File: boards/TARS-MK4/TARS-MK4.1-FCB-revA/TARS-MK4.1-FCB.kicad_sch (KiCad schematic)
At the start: 57 parts, among them J101 U.FL, J102 Molex_SlimStack_2091680401_2x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, J103 Molex_SlimStack_2091680401_2x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, J104 Molex_SlimStack_Plug_55091047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, J105 Molex_SlimStack_Plug_55091047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, J106 Conn_01x03, J107 Conn_01x02, J108 Conn_01x06, J109 Conn_01x03, Q101 SSM3K16FU, SW101 FSMSM Switch, U101 MS5611-01BA03, U102 LSM6DSLTR, U103 MAX-M10S, U104 BNO086, U105 LIS3MDL, U106 KX134-1211, U107 Teensy4.1, U108 BME688, Y101 32.768kHz

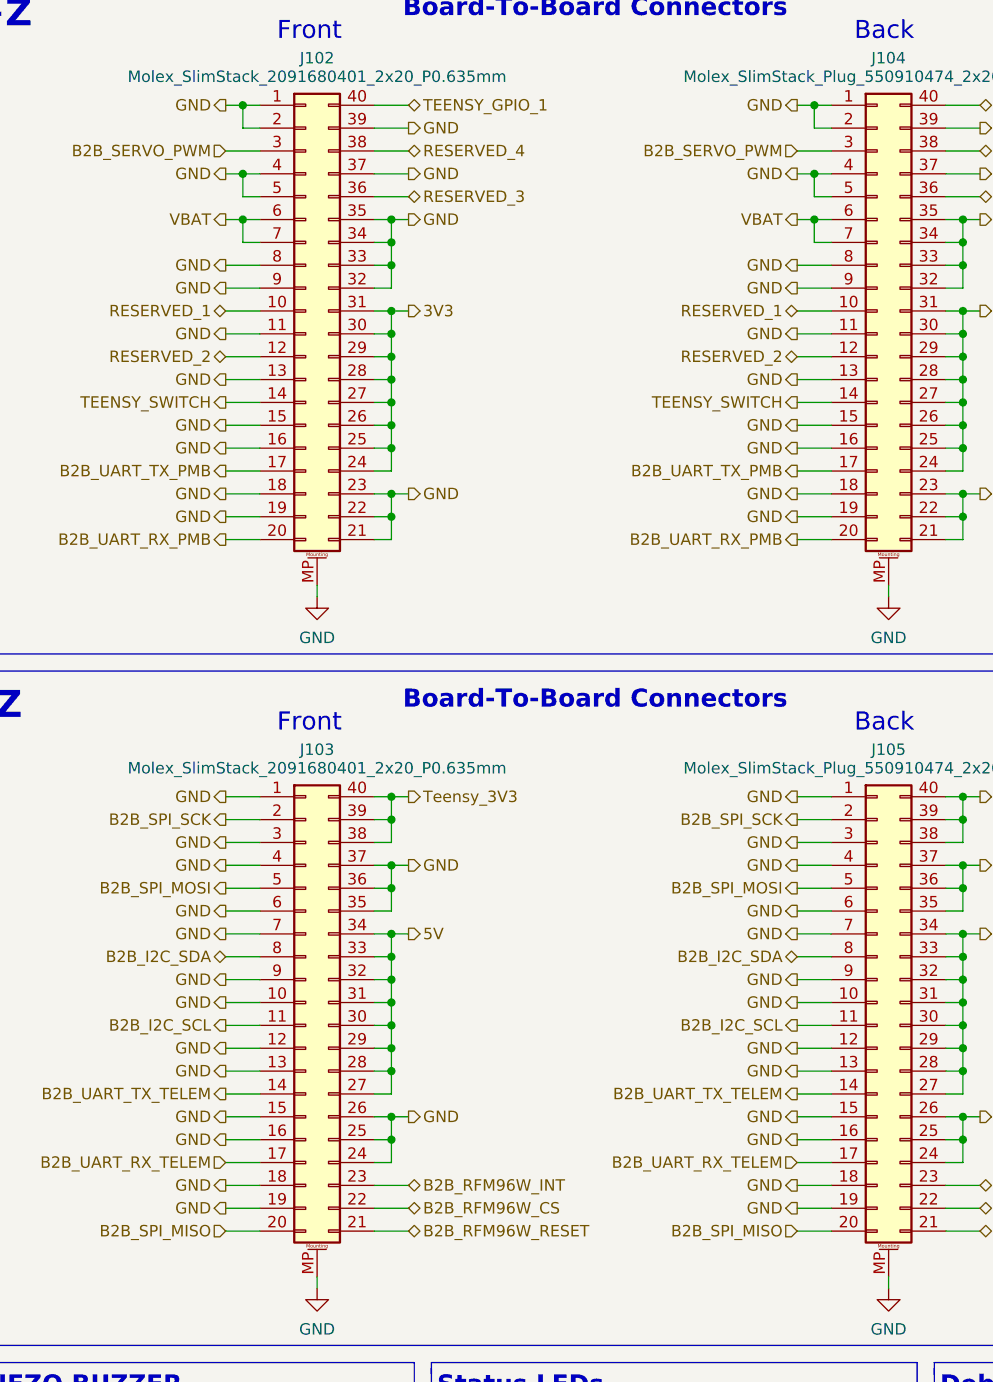
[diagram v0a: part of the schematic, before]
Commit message: Updated FCB B2B's to match PMB and TELEM
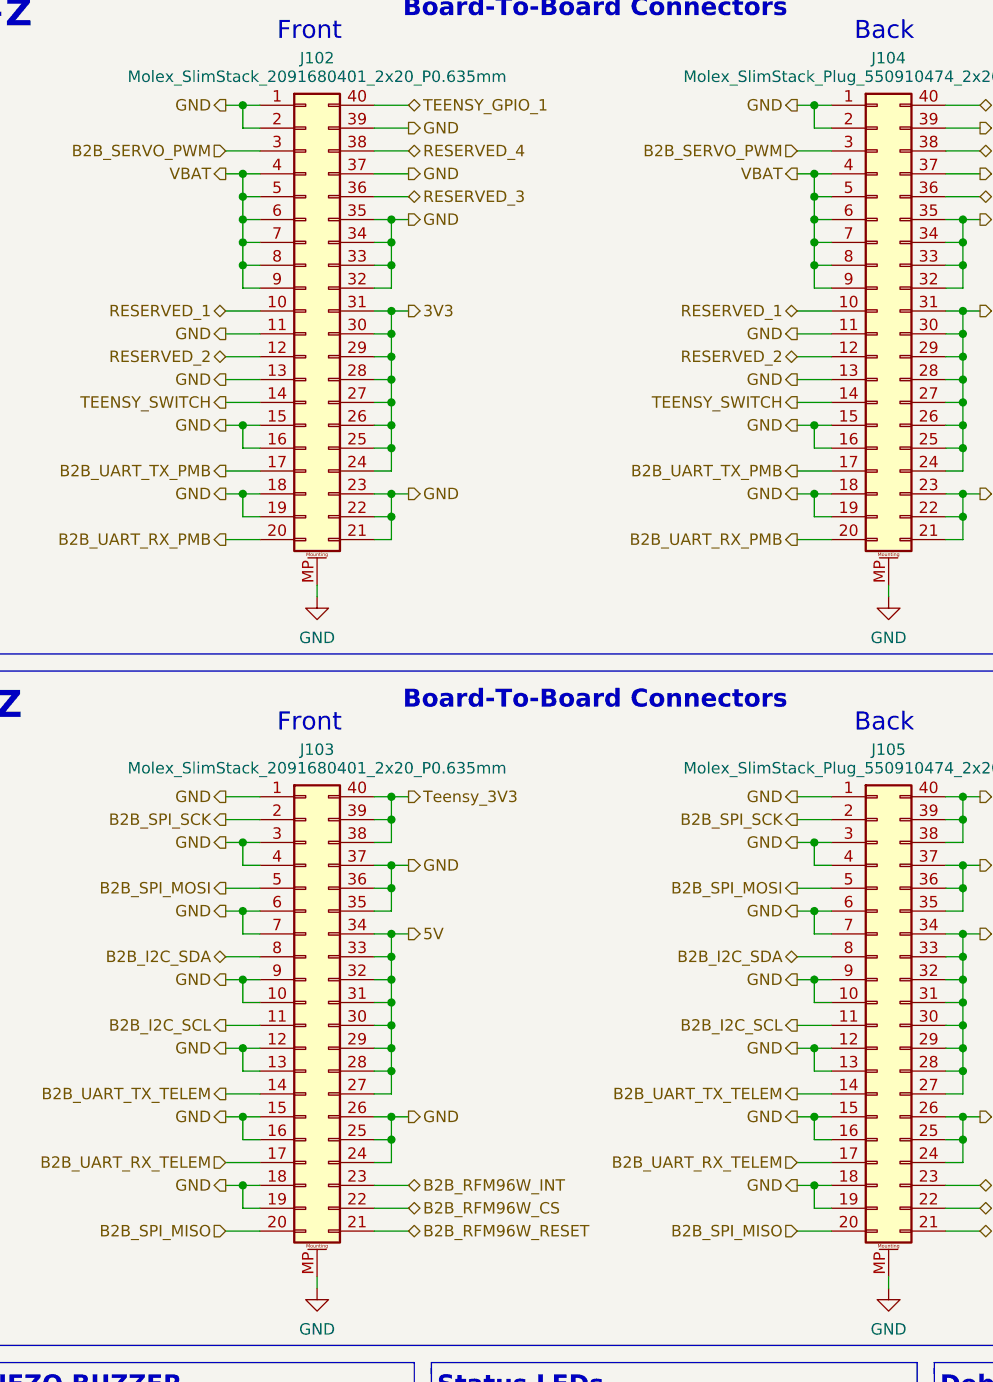
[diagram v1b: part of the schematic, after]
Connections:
- net GND: no longer J102.4 (Pin_4), J102.5 (Pin_5), J102.8 (Pin_8), J102.9 (Pin_9), J104.4 (Pin_4), J104.5 (Pin_5), J104.8 (Pin_8), J104.9 (Pin_9)
- net VBAT: now also J102.4 (Pin_4), J102.5 (Pin_5), J102.8 (Pin_8), J102.9 (Pin_9), J104.4 (Pin_4), J104.5 (Pin_5), J104.8 (Pin_8), J104.9 (Pin_9)
